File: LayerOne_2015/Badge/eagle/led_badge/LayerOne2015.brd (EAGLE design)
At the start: 68.6 x 68.2 mm, 72 parts, among them IC2 PQ1X331M2ZP-3V3-LDO-SOT-23-5, Q1 BSS138

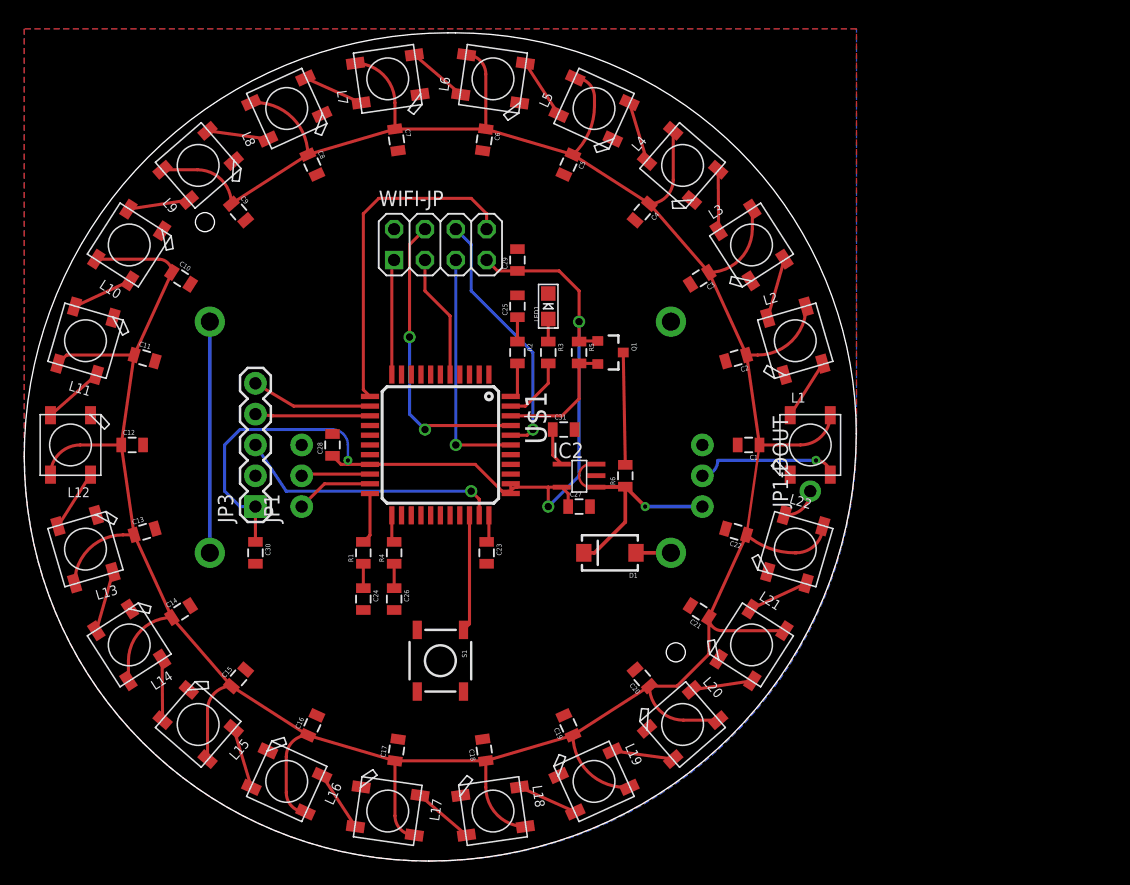
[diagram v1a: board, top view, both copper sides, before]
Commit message: 
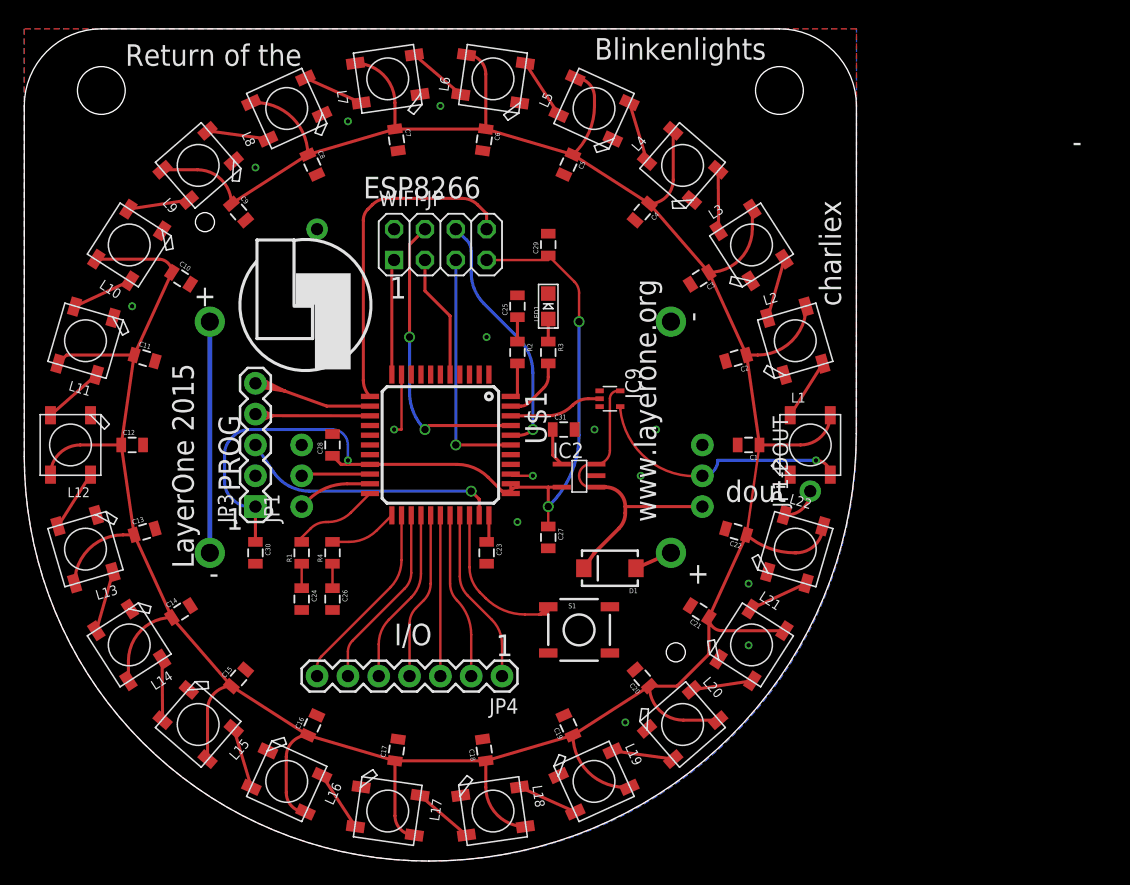
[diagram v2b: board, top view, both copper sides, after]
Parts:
- removed Q1: BSS138, SparkFun:SOT23-3
- removed R5, R6: 10K, SparkFun:0805
- added IC9: M74VHC1GT125DF2G, 74xx-little-de:SC70-5
- added JP4: (no value), SparkFun:1X07
- moved S1 11.7 mm to (11.4, -15.2), turned to 0 degrees
- moved C24 5.08 mm to (-11.4, -12.7)
- moved C26 5.08 mm to (-8.89, -12.7)
- moved R1 5.08 mm to (-11.4, -8.89)
- moved R4 5.08 mm to (-8.89, -8.89)
- moved C27 3.59 mm to (8.89, -7.62), turned to 270 degrees
- moved C29 2.84 mm to (8.89, 16.5)
- moved D1 1.27 mm to (14.0, -10.2)
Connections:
- removed net P1_5_5V: Q1.3, R6.2
- removed net P4_VDD: D1.C, IC2.1, IC2.3, JP2.1, R6.1
- new net N$29: JP4.7, U$1.24
- new net N$30: JP4.6, U$1.25
- new net N$31: JP4.5, U$1.26
- new net N$32: JP4.4, U$1.27
- new net N$33: JP4.3, U$1.28
- new net N$34: JP4.2, U$1.29
- new net N$35: JP4.1, U$1.30
- new net VCC: D1.C, IC2.1, IC2.3, IC9.5, JP2.1
- net 3.3V: no longer Q1.1, R5.1
- net DIN: now also IC9.4
- net GND: now also IC9.1, IC9.3
- net P1_5_3V: now also IC9.2; no longer Q1.2, R5.2
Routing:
- net VCC: track 0.00 -> 26.3 mm
- net P4_VDD: track 22.6 -> 0.00 mm, vias 1 -> 0
- net N$29: track 0.00 -> 15.8 mm
- net N$30: track 0.00 -> 15.2 mm
- net N$35: track 0.00 -> 14.4 mm
- net N$31: track 0.00 -> 14.3 mm
- net N$32: track 0.00 -> 13.7 mm
- net N$34: track 0.00 -> 13.6 mm
- net N$33: track 0.00 -> 13.2 mm
- net P1_5_5V: track 9.26 -> 0.00 mm
- net DIN: track 11.6 -> 20.5 mm
- net GND: track 0.00 -> 7.02 mm, vias 0 -> 14
- net P0_7: track 9.65 -> 15.6 mm
- net SWDIO: track 9.96 -> 15.3 mm
- net 3.3V: track 77.9 -> 74.0 mm
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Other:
- board size 68.6 x 68.2 mm -> 68.6 x 68.6 mm
- board text added: "+"
- board text added: "-"
- board text added: "1"
- board text added: "Blinkenlights"
- board text added: "ESP8266"
- board text added: "I/O"
- board text added: "LayerOne 2015"
- board text added: "PROG"
- board text added: "Return of the"
- board text added: "charliex"
- board text added: "dout"
- board text added: "www.layerone.org"

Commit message: 
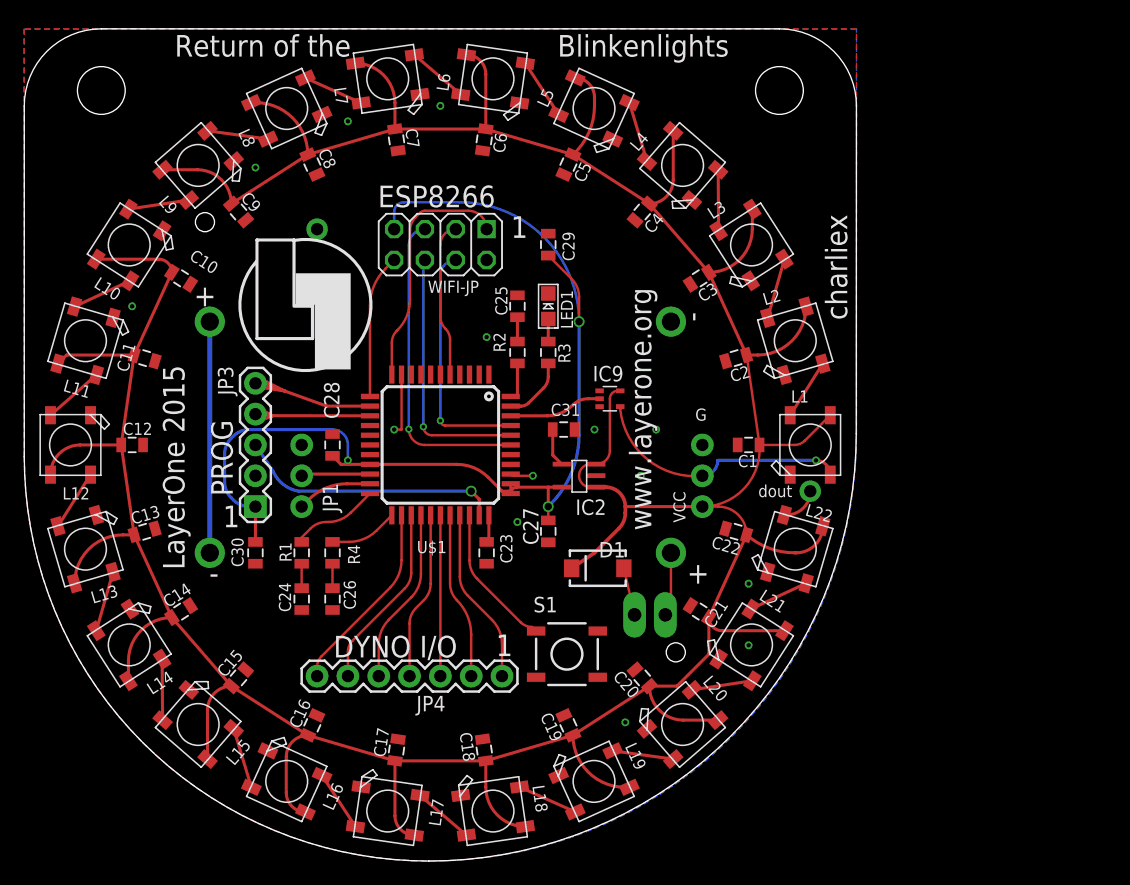
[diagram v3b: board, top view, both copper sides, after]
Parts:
- added JP5: M02PTH3, SparkFun-Connectors:1X02_LONGPADS
- moved S1 2.24 mm to (10.4, -17.2)
- moved D1 1.00 mm to (13.0, -10.2)
- moved C27 0.50 mm to (8.89, -7.12)
- turned WIFI-JP to 180 degrees
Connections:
- removed net VDD: C1.1, C10.1, C11.1, C12.1, C13.1, C14.1, C15.1, C16.1, C17.1, C18.1, C19.1, C2.1, C20.1, C21.1, C22.1, C3.1, C4.1, C5.1, C6.1, C7.1, C8.1, C9.1, L1.1-VDD, L10.1-VDD, L11.1-VDD, L12.1-VDD, L13.1-VDD, L14.1-VDD, L15.1-VDD, L16.1-VDD, L17.1-VDD, L18.1-VDD, L19.1-VDD, L2.1-VDD, L20.1-VDD, L21.1-VDD, L22.1-VDD, L3.1-VDD, L4.1-VDD, L5.1-VDD, L6.1-VDD, L7.1-VDD, L8.1-VDD, L9.1-VDD
- new net N$36: BAT1.+, JP5.2
- net BATTERY6V: now also JP5.1; no longer BAT1.+
- net VCC: now also C1.1, C10.1, C11.1, C12.1, C13.1, C14.1, C15.1, C16.1, C17.1, C18.1, C19.1, C2.1, C20.1, C21.1, C22.1, C3.1, C4.1, C5.1, C6.1, C7.1, C8.1, C9.1, L1.1-VDD, L10.1-VDD, L11.1-VDD, L12.1-VDD, L13.1-VDD, L14.1-VDD, L15.1-VDD, L16.1-VDD, L17.1-VDD, L18.1-VDD, L19.1-VDD, L2.1-VDD, L20.1-VDD, L21.1-VDD, L22.1-VDD, L3.1-VDD, L4.1-VDD, L5.1-VDD, L6.1-VDD, L7.1-VDD, L8.1-VDD, L9.1-VDD
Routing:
- net VCC: track 26.3 -> 339.6 mm
- net VDD: track 308.9 -> 0.00 mm
- net RX: track 27.3 -> 11.8 mm
- net 3.3V: track 74.0 -> 89.1 mm
- net TX: track 9.52 -> 20.0 mm
- net RST_3V: track 19.8 -> 26.0 mm
- net N$36: track 0.00 -> 5.30 mm
- net GPIO2_3V: track 24.5 -> 19.7 mm, vias 2 -> 1
- net P0_7: track 15.6 -> 11.9 mm
- net CH_PD: track 10.3 -> 12.7 mm
- net BATTERY6V: track 3.15 -> 3.94 mm
- net GPIO0_3V: track 20.5 -> 21.3 mm
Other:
- board text added: "DYNO I/O"
- board text added: "G"
- board text added: "VCC"
- board text removed: "I/O"

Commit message: 
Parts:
- moved C29 6.40 mm to (12.9, 11.5)
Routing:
- net 3.3V: track 89.1 -> 84.3 mm
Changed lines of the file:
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@@
 <layer number="14" name="Route14" color="1" fill="6" visible="no" active="no"/>
 <layer number="15" name="Route15" color="4" fill="6" visible="no" active="no"/>
-<layer number="16" name="Bottom" color="1" fill="1" visible="no" active="yes"/>
+<layer number="16" name="Bottom" color="1" fill="1" visible="yes" active="yes"/>
 <layer number="17" name="Pads" color="2" fill="1" visible="yes" active="yes"/>
-<layer number="18" name="Vias" color="2" fill="1" visible="no" active="yes"/>
-<layer number="19" name="Unrouted" color="6" fill="1" visible="no" active="yes"/>
+<layer number="18" name="Vias" color="2" fill="1" visible="yes" active="yes"/>
+<layer number="19" name="Unrouted" color="6" fill="1" visible="yes" active="yes"/>
 <layer number="20" name="Dimension" color="15" fill="1" visible="yes" active="yes"/>
 <layer number="21" name="tPlace" color="16" fill="1" visible="yes" active="yes"/>
-<layer number="22" name="bPlace" color="14" fill="1" visible="no" active="yes"/>
+<layer number="22" name="bPlace" color="14" fill="1" visible="yes" active="yes"/>
 <layer number="23" name="tOrigins" color="15" fill="1" visible="yes" active="yes"/>
-<layer number="24" name="bOrigins" color="15" fill="1" visible="no" active="yes"/>
+<layer number="24" name="bOrigins" color="15" fill="1" visible="yes" active="yes"/>
 <layer number="25" name="tNames" color="7" fill="1" visible="yes" active="yes"/>
 <layer number="26" name="bNames" color="7" fill="1" visible="no" active="yes"/>
@@
 <attribute name="VALUE" x="-7.874" y="1.905" size="0.4064" layer="27" rot="R180"/>
 </element>
-<element name="C29" library="SparkFun-Capacitors" package="0805" value="0.1uF" x="8.89" y="16.51" smashed="yes" rot="R90">
-<attribute name="NAME" x="11.0645" y="15.148" size="1" layer="25" rot="R90"/>
-<attribute name="VALUE" x="10.287" y="15.494" size="0.4064" layer="27" rot="R90"/>
+<element name="C29" library="SparkFun-Capacitors" package="0805" value="0.1uF" x="12.89" y="11.51" smashed="yes" rot="R90">
+<attribute name="NAME" x="15.0645" y="10.148" size="1" layer="25" rot="R90"/>
+<attribute name="VALUE" x="14.287" y="10.494" size="0.4064" layer="27" rot="R90"/>
 </element>
 <element name="C3" library="SparkFun-Passives" package="0805" value="" x="21.367840625" y="13.732278125" smashed="yes" rot="R212.7">
@@
 <via x="-7.62" y="-1.27" extent="1-16" drill="0.3556"/>
 <wire x1="-7.62" y1="-1.27" x2="-7.62" y2="-1.6" width="0.2032" layer="1"/>
-<wire x1="8.89" y1="15.61" x2="10.82246875" y2="13.67753125" width="0.2032" layer="1"/>
-<wire x1="10.82246875" y1="13.67753125" x2="11.43" y2="12.21081875" width="0.2032" layer="1" curve="-45"/>
-<wire x1="11.43" y1="12.21081875" x2="11.43" y2="10.16" width="0.2032" layer="1"/>
 <wire x1="8.89" y1="-5.08" x2="8.89" y2="-6.22" width="0.2032" layer="1"/>
 <wire x1="-3.81" y1="17.78" x2="-3.81" y2="19.19" width="0.2032" layer="16"/>
@@
 <wire x1="-3" y1="20" x2="1.59" y2="20" width="0.2032" layer="16"/>
 <wire x1="1.59" y1="20" x2="11.43" y2="10.16" width="0.2032" layer="16" curve="-90"/>
+<wire x1="12.89" y1="10.61" x2="11.88" y2="10.61" width="0.2032" layer="1"/>
+<wire x1="11.88" y1="10.61" x2="11.43" y2="10.16" width="0.2032" layer="1"/>
 </signal>
 <signal name="VCCD">
